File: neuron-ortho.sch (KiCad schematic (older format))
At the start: 130 parts, among them J1 USB_C_Receptacle_USB2.0, J2 Conn_01x04_Male, J3 Conn_01x06_Male, Q1 DTC123J, SW1 SW_Push, U1 STM32F303C6Tx, U2 NCP1117-3.3_SOT223, Y1 8MHz

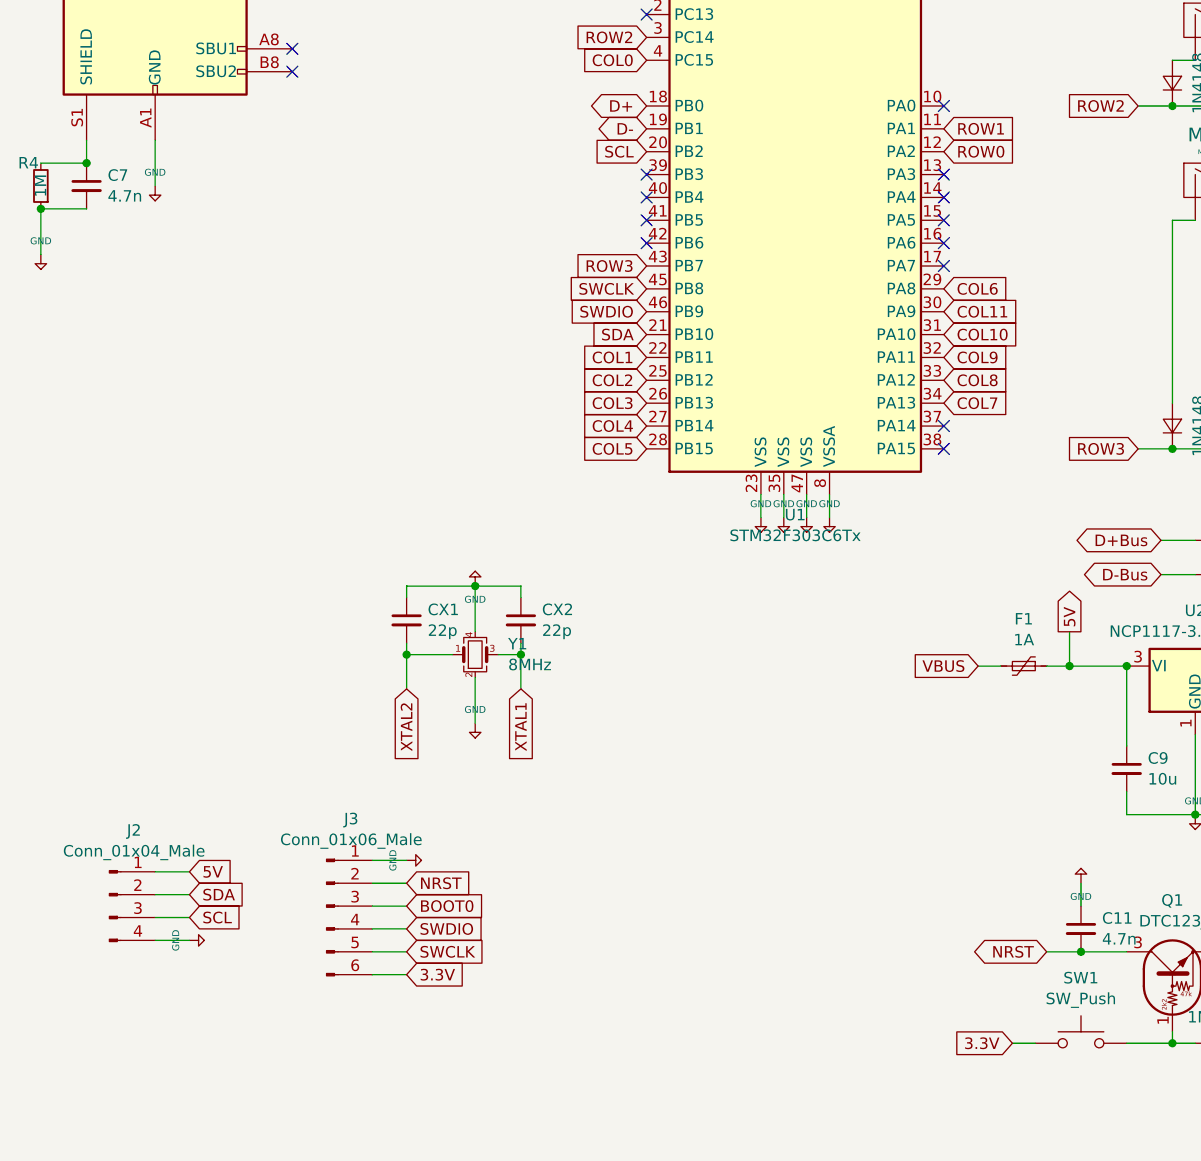
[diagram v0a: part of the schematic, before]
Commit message: Updated pin out footprint
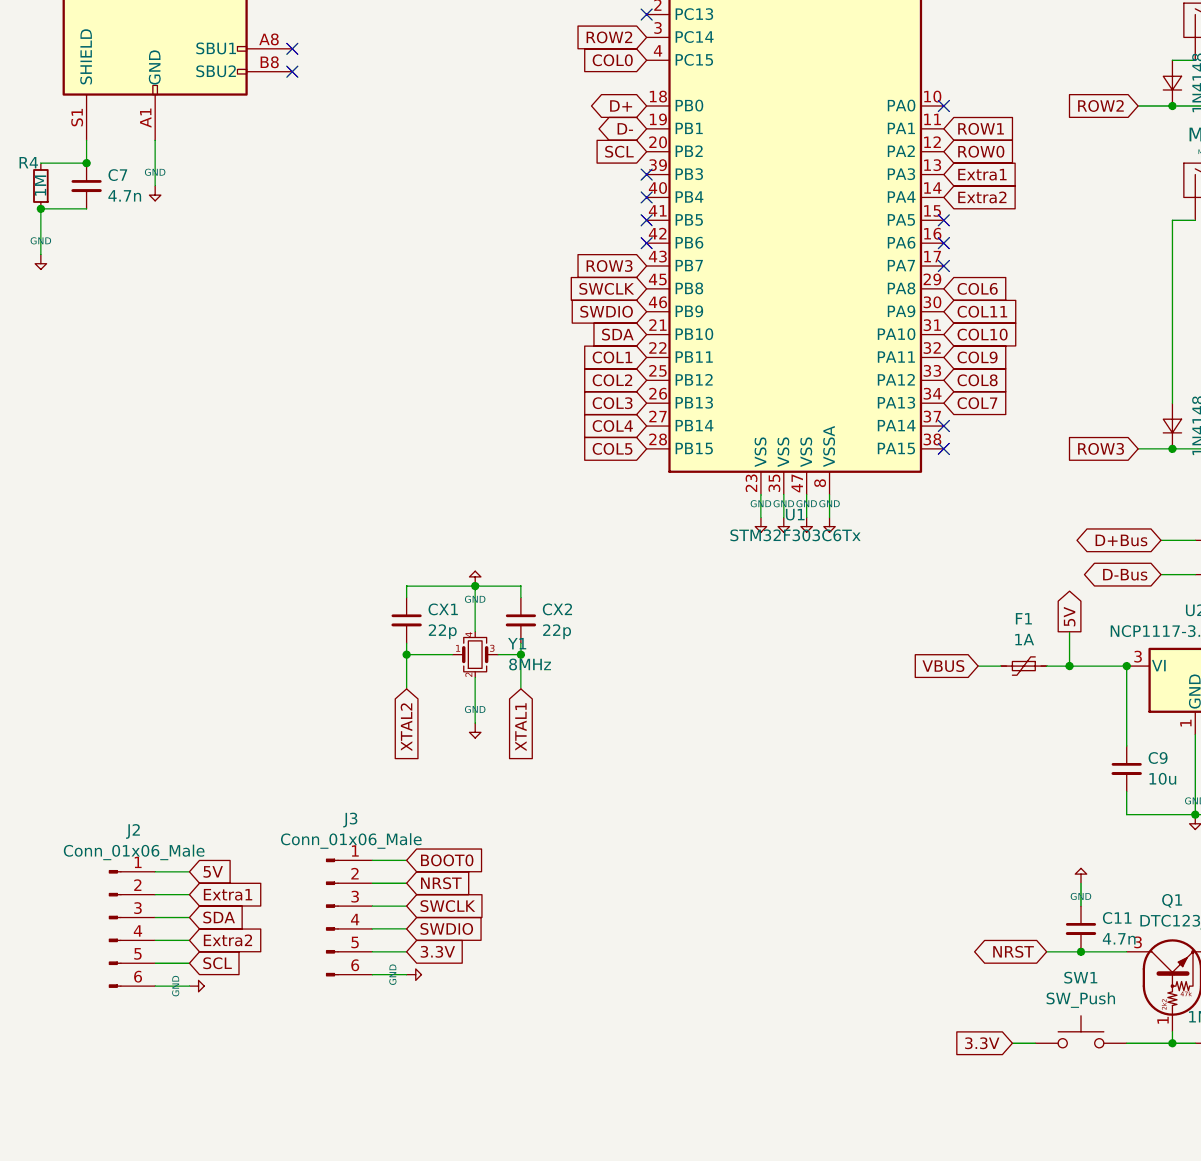
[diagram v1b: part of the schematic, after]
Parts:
- removed J2: Conn_01x04_Male, Connector_PinSocket_1.00mm:PinSocket_1x04_P1.00mm_Vertical, symbol Connector:Conn_01x04_Male
- added J2: Conn_01x06_Male, random-keyboard-parts:Reset_Pretty, symbol Connector:Conn_01x06_Male
- J3: footprint Connector_PinSocket_1.00mm:PinSocket_1x06_P1.00mm_Vertical -> random-keyboard-parts:Reset_Pretty
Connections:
- net +5V: now also J3.6 (Pin_6), J2.6 (Pin_6); no longer J3.1 (Pin_1)
- net 3.3V: now also J3.5 (Pin_5); no longer J3.6 (Pin_6)
- net 5V: now also J2.1 (Pin_1)
- net BOOT0: now also J3.1 (Pin_1); no longer J3.3 (Pin_3)
- net SCL: now also J2.5 (Pin_5)
- net SDA: now also J2.3 (Pin_3)
- net SWCLK: now also J3.3 (Pin_3); no longer J3.5 (Pin_5)
- net Extra1: now reaches U1.13 (PA3)
- net Extra1: now also J2.2 (Pin_2)
- net Extra2: now reaches U1.14 (PA4)
- net Extra2: now also J2.4 (Pin_4)
- no-connect marks 15 -> 13
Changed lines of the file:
@@
 	2300 2350 2400 2350
-$Comp
-L Connector:Conn_01x04_Male J2
-U 1 1 5E754717
-P 1000 6350
-F 0 "J2" H 1108 6631 50  0000 C CNN
-F 1 "Conn_01x04_Male" H 1108 6540 50  0000 C CNN
-F 2 "Connector_PinSocket_1.00mm:PinSocket_1x04_P1.00mm_Vertical" H 1000 6350 50  0001 C CNN
-F 3 "~" H 1000 6350 50  0001 C CNN
-	1    1000 6350
-	1    0    0    -1
-$EndComp
 $Comp
 L Connector:Conn_01x06_Male J3
@@
 F 0 "J3" H 2058 6781 50  0000 C CNN
 F 1 "Conn_01x06_Male" H 2058 6690 50  0000 C CNN
-F 2 "Connector_PinSocket_1.00mm:PinSocket_1x06_P1.00mm_Vertical" H 1950 6400 50  0001 C CNN
+F 2 "random-keyboard-parts:Reset_Pretty" H 1950 6400 50  0001 C CNN
 F 3 "~" H 1950 6400 50  0001 C CNN
 	1    1950 6400
@@
 L keyboard_parts:GND #PWR0101
 U 1 1 5E796914
-P 1350 6550
-F 0 "#PWR0101" H 1350 6600 20  0001 C CNN
-F 1 "GND" H 1350 6609 30  0000 C CNN
-F 2 "" H 1350 6550 60  0000 C CNN
-F 3 "" H 1350 6550 60  0000 C CNN
-	1    1350 6550
+P 1350 6750
+F 0 "#PWR0101" H 1350 6800 20  0001 C CNN
+F 1 "GND" H 1350 6809 30  0000 C CNN
+F 2 "" H 1350 6750 60  0000 C CNN
+F 3 "" H 1350 6750 60  0000 C CNN
+	1    1350 6750
 	0    -1   -1   0
 $EndComp
@@
 L keyboard_parts:GND #PWR0102
 U 1 1 5E79741B
-P 2300 6200
-F 0 "#PWR0102" H 2300 6250 20  0001 C CNN
-F 1 "GND" H 2300 6259 30  0000 C CNN
-F 2 "" H 2300 6200 60  0000 C CNN
-F 3 "" H 2300 6200 60  0000 C CNN
-	1    2300 6200
+P 2300 6700
+F 0 "#PWR0102" H 2300 6750 20  0001 C CNN
+F 1 "GND" H 2300 6759 30  0000 C CNN
+F 2 "" H 2300 6700 60  0000 C CNN
+F 3 "" H 2300 6700 60  0000 C CNN
+	1    2300 6700
 	0    -1   -1   0
 $EndComp
 Text GLabel 1350 6250 2    50   Input ~ 0
 5V
-Text GLabel 1350 6350 2    50   Input ~ 0
+Text GLabel 1350 6450 2    50   Input ~ 0
 SDA
-Text GLabel 1350 6450 2    50   Input ~ 0
+Text GLabel 1350 6650 2    50   Input ~ 0
 SCL
 Text GLabel 2300 6300 2    50   Input ~ 0
 NRST
-Text GLabel 2300 6700 2    50   Input ~ 0
+Text GLabel 2300 6600 2    50   Input ~ 0
 3.3V
 Wire Wire Line
@@
 	1200 6450 1350 6450
 Wire Wire Line
-	1200 6550 1350 6550
+	1200 6750 1350 6750
 Wire Wire Line
 	2150 6200 2300 6200
@@
 	6100 3750 6100 4200
 NoConn ~ 3350 3200
-NoConn ~ 4650 3200
 NoConn ~ 3350 3300
 NoConn ~ 3350 3400
 NoConn ~ 3350 3500
-NoConn ~ 4650 3300
 NoConn ~ 4650 3400
 NoConn ~ 4650 3500
@@
 	0    -1   -1   0
 $EndComp
-Text GLabel 2300 6600 2    50   Input ~ 0
+Text GLabel 2300 6400 2    50   Input ~ 0
 SWCLK
 Text GLabel 2300 6500 2    50   Input ~ 0
 SWDIO
-Text GLabel 2300 6400 2    50   Input ~ 0
+Text GLabel 2300 6200 2    50   Input ~ 0
 BOOT0
 Text GLabel 4950 7000 0    50   Input ~ 0
@@
 NoConn ~ 4650 2900
 NoConn ~ 3350 2500
+$Comp
+L Connector:Conn_01x06_Male J2
+U 1 1 5E763C45
+P 1000 6450
+F 0 "J2" H 1108 6831 50  0000 C CNN
+F 1 "Conn_01x06_Male" H 1108 6740 50  0000 C CNN
+F 2 "random-keyboard-parts:Reset_Pretty" H 1000 6450 50  0001 C CNN
+F 3 "~" H 1000 6450 50  0001 C CNN
+	1    1000 6450
+	1    0    0    -1
+$EndComp
+Text GLabel 1350 6350 2    50   Input ~ 0
+Extra1
+Text GLabel 1350 6550 2    50   Input ~ 0
+Extra2
+Wire Wire Line
+	1200 6550 1350 6550
+Wire Wire Line
+	1200 6650 1350 6650
+Text GLabel 4650 3200 2    50   Input ~ 0
+Extra1
+Text GLabel 4650 3300 2    50   Input ~ 0
+Extra2
 $EndSCHEMATC
